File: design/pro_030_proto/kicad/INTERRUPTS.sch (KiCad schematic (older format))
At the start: 11 parts, among them IC25 74LS148

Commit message: Big(ish) push on placement
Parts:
- C55: footprint rosco_m68k:C2.5-3 -> Capacitor_THT:C_Rect_L4.0mm_W2.5mm_P2.50mm
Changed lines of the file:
@@
 F 0 "C55" H 8210 3765 59  0000 L BNN
 F 1 "100nF" H 8210 3565 59  0000 L BNN
-F 2 "rosco_m68k:C2.5-3" H 8150 3750 50  0001 C CNN
+F 2 "Capacitor_THT:C_Rect_L4.0mm_W2.5mm_P2.50mm" H 8150 3750 50  0001 C CNN
 F 3 "" H 8150 3750 50  0001 C CNN
 	1    8150 3750

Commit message: Further layout
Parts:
- renumbered C55 to C62, IC25 to IC28, R60 to R74, R61 to R75, R62 to R76, R63 to R77, R64 to R78, R65 to R79, R66 to R80, R67 to R81, R68 to R82
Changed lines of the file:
@@
 AR Path="/5E53B952/611FB0FB" Ref="C?"  Part="1"
 AR Path="/60FBFA5C/611FB0FB" Ref="C?"  Part="1"
-AR Path="/611F7BD0/611FB0FB" Ref="C55"  Part="1"
-F 0 "C55" H 8210 3765 59  0000 L BNN
+AR Path="/611F7BD0/611FB0FB" Ref="C62"  Part="1"
+F 0 "C62" H 8210 3765 59  0000 L BNN
 F 1 "100nF" H 8210 3565 59  0000 L BNN
 F 2 "Capacitor_THT:C_Rect_L4.0mm_W2.5mm_P2.50mm" H 8150 3750 50  0001 C CNN
@@
 	6450 4850 6450 4900
 $Comp
-L power:GND #PWR049
+L power:GND #PWR048
 U 1 1 611FB103
 P 6450 4950
-F 0 "#PWR049" H 6450 4700 50  0001 C CNN
+F 0 "#PWR048" H 6450 4700 50  0001 C CNN
 F 1 "GND" H 6455 4777 50  0000 C CNN
 F 2 "" H 6450 4950 50  0001 C CNN
@@
 $EndComp
 $Comp
-L power:VCC #PWR048
+L power:VCC #PWR047
 U 1 1 611FB109
 P 6450 2550
-F 0 "#PWR048" H 6450 2400 50  0001 C CNN
+F 0 "#PWR047" H 6450 2400 50  0001 C CNN
 F 1 "VCC" H 6467 2723 50  0000 C CNN
 F 2 "" H 6450 2550 50  0001 C CNN
@@
 P 6450 3050
 AR Path="/60FBFA5C/611FB118" Ref="R?"  Part="1"
-AR Path="/611F7BD0/611FB118" Ref="R67"  Part="1"
-F 0 "R67" H 6520 3096 50  0000 L CNN
+AR Path="/611F7BD0/611FB118" Ref="R81"  Part="1"
+F 0 "R81" H 6520 3096 50  0000 L CNN
 F 1 "4K7" H 6520 3005 50  0000 L CNN
 F 2 "rosco_m68k:R-0207_10" V 6380 3050 50  0001 C CNN
@@
 P 6450 4700
 AR Path="/60FBFA5C/611FB11E" Ref="R?"  Part="1"
-AR Path="/611F7BD0/611FB11E" Ref="R68"  Part="1"
-F 0 "R68" H 6520 4746 50  0000 L CNN
+AR Path="/611F7BD0/611FB11E" Ref="R82"  Part="1"
+F 0 "R82" H 6520 4746 50  0000 L CNN
 F 1 "4K7" H 6520 4655 50  0000 L CNN
 F 2 "rosco_m68k:R-0207_10" V 6380 4700 50  0001 C CNN
@@
 NoConn ~ 7650 4000
 $Comp
-L 74xx:74LS148 IC25
+L 74xx:74LS148 IC28
 U 1 1 611FB12D
 P 7150 3900
-F 0 "IC25" H 7150 4781 50  0000 C CNN
+F 0 "IC28" H 7150 4781 50  0000 C CNN
 F 1 "74LS148" H 7150 4690 50  0000 C CNN
 F 2 "Package_DIP:DIP-16_W7.62mm_Socket_LongPads" H 7150 3900 50  0001 C CNN
@@
 P 6150 3050
 AR Path="/60FBFA5C/611FB7DD" Ref="R?"  Part="1"
-AR Path="/611F7BD0/611FB7DD" Ref="R66"  Part="1"
-F 0 "R66" H 6220 3096 50  0000 L CNN
+AR Path="/611F7BD0/611FB7DD" Ref="R80"  Part="1"
+F 0 "R80" H 6220 3096 50  0000 L CNN
 F 1 "2K2" H 6220 3005 50  0000 L CNN
 F 2 "rosco_m68k:R-0207_10" V 6080 3050 50  0001 C CNN
@@
 P 5850 3050
 AR Path="/60FBFA5C/611FBFF4" Ref="R?"  Part="1"
-AR Path="/611F7BD0/611FBFF4" Ref="R65"  Part="1"
-F 0 "R65" H 5920 3096 50  0000 L CNN
+AR Path="/611F7BD0/611FBFF4" Ref="R79"  Part="1"
+F 0 "R79" H 5920 3096 50  0000 L CNN
 F 1 "2K2" H 5920 3005 50  0000 L CNN
 F 2 "rosco_m68k:R-0207_10" V 5780 3050 50  0001 C CNN
@@
 P 5550 3050
 AR Path="/60FBFA5C/611FC4E3" Ref="R?"  Part="1"
-AR Path="/611F7BD0/611FC4E3" Ref="R64"  Part="1"
-F 0 "R64" H 5620 3096 50  0000 L CNN
+AR Path="/611F7BD0/611FC4E3" Ref="R78"  Part="1"
+F 0 "R78" H 5620 3096 50  0000 L CNN
 F 1 "2K2" H 5620 3005 50  0000 L CNN
 F 2 "rosco_m68k:R-0207_10" V 5480 3050 50  0001 C CNN
@@
 P 5250 3050
 AR Path="/60FBFA5C/611FCAF8" Ref="R?"  Part="1"
-AR Path="/611F7BD0/611FCAF8" Ref="R63"  Part="1"
-F 0 "R63" H 5320 3096 50  0000 L CNN
+AR Path="/611F7BD0/611FCAF8" Ref="R77"  Part="1"
+F 0 "R77" H 5320 3096 50  0000 L CNN
 F 1 "2K2" H 5320 3005 50  0000 L CNN
 F 2 "rosco_m68k:R-0207_10" V 5180 3050 50  0001 C CNN
@@
 P 4950 3050
 AR Path="/60FBFA5C/611FD2C6" Ref="R?"  Part="1"
-AR Path="/611F7BD0/611FD2C6" Ref="R62"  Part="1"
-F 0 "R62" H 5020 3096 50  0000 L CNN
+AR Path="/611F7BD0/611FD2C6" Ref="R76"  Part="1"
+F 0 "R76" H 5020 3096 50  0000 L CNN
 F 1 "2K2" H 5020 3005 50  0000 L CNN
 F 2 "rosco_m68k:R-0207_10" V 4880 3050 50  0001 C CNN
@@
 P 4650 3050
 AR Path="/60FBFA5C/611FD92F" Ref="R?"  Part="1"
-AR Path="/611F7BD0/611FD92F" Ref="R61"  Part="1"
-F 0 "R61" H 4720 3096 50  0000 L CNN
+AR Path="/611F7BD0/611FD92F" Ref="R75"  Part="1"
+F 0 "R75" H 4720 3096 50  0000 L CNN
 F 1 "2K2" H 4720 3005 50  0000 L CNN
 F 2 "rosco_m68k:R-0207_10" V 4580 3050 50  0001 C CNN
@@
 P 4350 3050
 AR Path="/60FBFA5C/611FDE09" Ref="R?"  Part="1"
-AR Path="/611F7BD0/611FDE09" Ref="R60"  Part="1"
-F 0 "R60" H 4420 3096 50  0000 L CNN
+AR Path="/611F7BD0/611FDE09" Ref="R74"  Part="1"
+F 0 "R74" H 4420 3096 50  0000 L CNN
 F 1 "2K2" H 4420 3005 50  0000 L CNN
 F 2 "rosco_m68k:R-0207_10" V 4280 3050 50  0001 C CNN

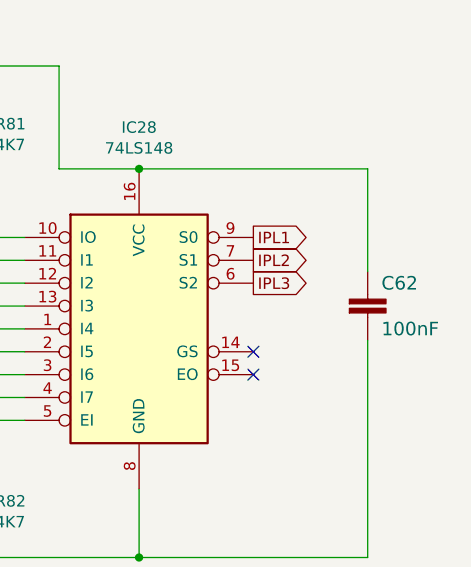
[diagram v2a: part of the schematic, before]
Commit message: Add IO and XVID glue etc.
* Add IO Select glue
* Add Xosera glue
* Add new glues to schematic
* Clean up libs
* Reannotate (again)
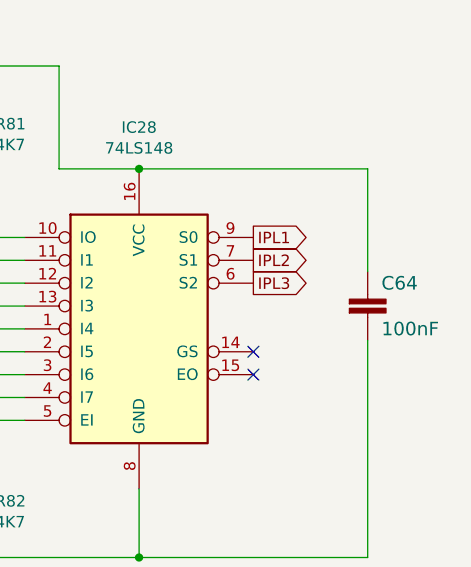
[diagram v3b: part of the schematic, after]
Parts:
- renumbered C62 to C64
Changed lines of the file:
@@
 AR Path="/5E53B952/611FB0FB" Ref="C?"  Part="1"
 AR Path="/60FBFA5C/611FB0FB" Ref="C?"  Part="1"
-AR Path="/611F7BD0/611FB0FB" Ref="C62"  Part="1"
-F 0 "C62" H 8210 3765 59  0000 L BNN
+AR Path="/611F7BD0/611FB0FB" Ref="C64"  Part="1"
+F 0 "C64" H 8210 3765 59  0000 L BNN
 F 1 "100nF" H 8210 3565 59  0000 L BNN
 F 2 "Capacitor_THT:C_Rect_L4.0mm_W2.5mm_P2.50mm" H 8150 3750 50  0001 C CNN
@@
 	6450 4850 6450 4900
 $Comp
-L power:GND #PWR048
+L power:GND #PWR050
 U 1 1 611FB103
 P 6450 4950
-F 0 "#PWR048" H 6450 4700 50  0001 C CNN
+F 0 "#PWR050" H 6450 4700 50  0001 C CNN
 F 1 "GND" H 6455 4777 50  0000 C CNN
 F 2 "" H 6450 4950 50  0001 C CNN
@@
 $EndComp
 $Comp
-L power:VCC #PWR047
+L power:VCC #PWR049
 U 1 1 611FB109
 P 6450 2550
-F 0 "#PWR047" H 6450 2400 50  0001 C CNN
+F 0 "#PWR049" H 6450 2400 50  0001 C CNN
 F 1 "VCC" H 6467 2723 50  0000 C CNN
 F 2 "" H 6450 2550 50  0001 C CNN

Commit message: Finally fix ERC...
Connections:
- net IPL3 is gone; now on net IPL2: IC28.6 (S2)
- net IPL1: now also IC28.7 (S1); no longer IC28.9 (S0)
- net IPL2: no longer IC28.7 (S1)
- new net IPL0: IC28.9 (S0)
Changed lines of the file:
@@
 Connection ~ 6450 2750
 Text GLabel 7650 3700 2    50   Output ~ 0
-IPL3
+IPL2
 Text GLabel 7650 3600 2    50   Output ~ 0
-IPL2
+IPL1
 Text GLabel 7650 3500 2    50   Output ~ 0
-IPL1
+IPL0
 Connection ~ 7150 4900
 Wire Wire Line
